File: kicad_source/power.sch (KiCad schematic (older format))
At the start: 19 parts, among them Q1 2N7002, Q2 2N7002, Q5 NTR4171P, SW3 SWITCH_INV, U1 TPS383X, U2 MCP73831, U3 TPS736XX

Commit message: updated power circuit
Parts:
- removed C1: 1u, capacitors:C_0603, symbol devices:C_0603
- removed D1: yellow, LEDs:LED_0603, symbol devices:Led_Small
- removed D5: MBR120, diodes:SOD-123, symbol devices:D_Schottky_Small
- removed F1: SF-1206S050, fuse_holders_and_fuses:Fuse_SMD1206_Reflow, symbol devices:F_Small
- removed Q1, Q2: 2N7002, SOT_TO:SOT-23, symbol devices:Q_NMOS_GSD
- removed Q5: NTR4171P, SOT_TO:SOT-23, symbol devices:Q_PMOS_GSD
- removed R1, R24: 4k7, resistors:R_0603, symbol devices:R_1206
- removed R5: 10k, resistors:R_0603, symbol devices:R_1206
- removed R7: 2k5, resistors:R_0603, symbol devices:R_1206
- removed U1: TPS383X, SOT_TO:SOT-23, symbol IC_voltage_supervisor:TPS383X
- removed U2: MCP73831, SOT_TO:SOT-23-5, symbol IC_batterycharger:MCP73831
- added BT?: Keystone 1043, MECH_battery_holder:KEYSTONE_1043, symbol devices:Battery
- added C? (x3): 1u, capacitors:C_0603, symbol devices:C_0603
- added C?: 100u/6.3V, capacitors:TantalC_SizeD_EIA-7343_Reflow, symbol devices:CP_Small
- added D? (x2): D_Small, symbol devices:D_Small
- added D?: D_Schottky_Small, symbol devices:D_Schottky_Small
- added R?: 150k, resistors:R_0603, symbol devices:R_0603
- added U?: TPS736XX, SOT_TO:SOT-23-5, symbol voltage-regulators:TPS736XX
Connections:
- net labels added: +1V8, 1V8_EN, VDD_CORE_EN
- net labels removed: +BATT, CHR_100MA, CHR_500MA, PROG
- wire segments 57 -> 46
- no-connect marks 2 -> 3
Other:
- note added: "use TPS73618DBVT\nfixed voltage 1.8 V"
- note added: "use TPS73633DBVT\nfixed voltage 3.3 V"
- note removed: "use MCP73832-2ACI/OT (4.2 V)"
- note removed: "use TPS3839G33DBZR\nthreshold voltage 3.08 V"
- note removed: "use TPS73630DBVT\nfixed voltage 3.0 V"
- moved on the sheet: BT1, C12, C2, C7, SW3, U3

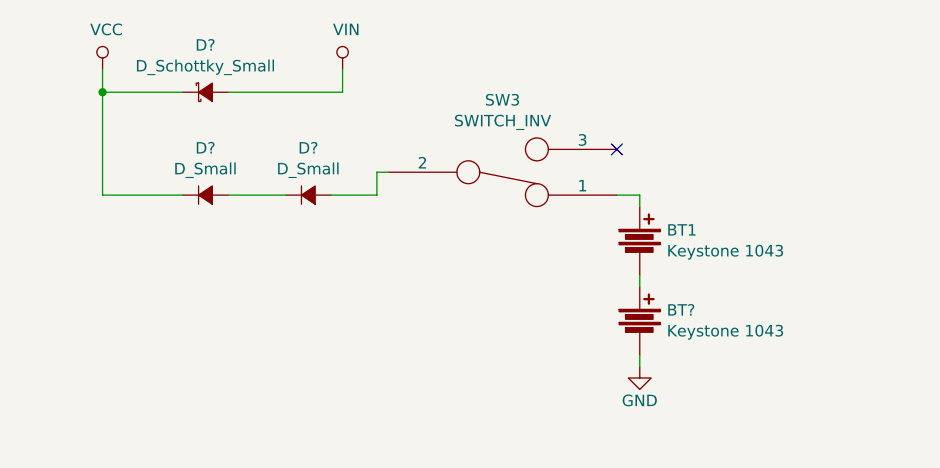
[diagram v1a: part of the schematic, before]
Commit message: added flash, JTAG connector and display to schematic
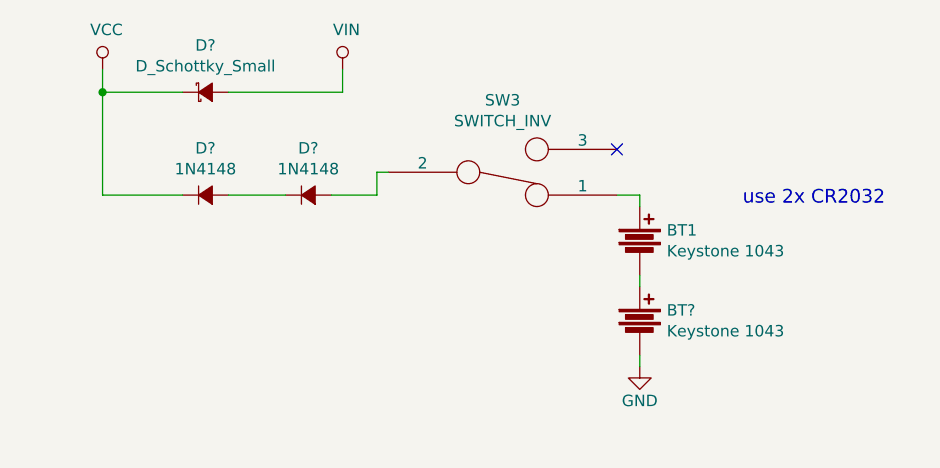
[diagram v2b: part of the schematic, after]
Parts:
- D? (x2): value D_Small -> 1N4148
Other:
- note added: "use 2x CR2032"
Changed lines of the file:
@@
 P 5500 1800
 F 0 "D?" H 5500 2005 50  0000 C CNN
-F 1 "D_Small" H 5500 1914 50  0000 C CNN
+F 1 "1N4148" H 5500 1914 50  0000 C CNN
 F 2 "" V 5500 1800 50  0000 C CNN
 F 3 "" V 5500 1800 50  0000 C CNN
@@
 P 5050 1800
 F 0 "D?" H 5050 2005 50  0000 C CNN
-F 1 "D_Small" H 5050 1914 50  0000 C CNN
+F 1 "1N4148" H 5050 1914 50  0000 C CNN
 F 2 "" V 5050 1800 50  0000 C CNN
 F 3 "" V 5050 1800 50  0000 C CNN
@@
 Wire Wire Line
 	6950 2500 6950 2550
+Text Notes 7400 1850 0    60   ~ 0
+use 2x CR2032
 $EndSCHEMATC

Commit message: added nfc part, generated schematic pdf
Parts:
- gave numbers to parts that had none: 10
- renumbered C2 to C32, C7 to C35, C12 to C37, SW3 to SW5, U3 to U5

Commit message: started placement
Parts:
- D7: value D_Schottky_Small -> MBR0530; footprint (none) -> diodes:SOD-123
- D8, D9: footprint (none) -> diodes:SOD-123
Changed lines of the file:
@@
 F 0 "D9" H 5500 2005 50  0000 C CNN
 F 1 "1N4148" H 5500 1914 50  0000 C CNN
-F 2 "" V 5500 1800 50  0000 C CNN
+F 2 "diodes:SOD-123" V 5500 1800 50  0001 C CNN
 F 3 "" V 5500 1800 50  0000 C CNN
 	1    5500 1800
@@
 F 0 "D8" H 5050 2005 50  0000 C CNN
 F 1 "1N4148" H 5050 1914 50  0000 C CNN
-F 2 "" V 5050 1800 50  0000 C CNN
+F 2 "diodes:SOD-123" V 5050 1800 50  0001 C CNN
 F 3 "" V 5050 1800 50  0000 C CNN
 	1    5050 1800
@@
 P 5050 1350
 F 0 "D7" H 5050 1555 50  0000 C CNN
-F 1 "D_Schottky_Small" H 5050 1464 50  0000 C CNN
-F 2 "" V 5050 1350 50  0000 C CNN
+F 1 "MBR0530" H 5050 1464 50  0000 C CNN
+F 2 "diodes:SOD-123" V 5050 1350 50  0001 C CNN
 F 3 "" V 5050 1350 50  0000 C CNN
 	1    5050 1350

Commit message: made first placement
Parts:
- BT1, BT2: value Keystone 1043 -> 79523141; footprint MECH_battery_holder:KEYSTONE_1043 -> MECH_battery_holder:Wuerth_WA-BCMC_79523141
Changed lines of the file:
@@
 AR Path="/5EB35F1D/5CB4F961" Ref="BT1"  Part="1"
 F 0 "BT1" H 7068 2046 50  0000 L CNN
-F 1 "Keystone 1043" H 7068 1955 50  0000 L CNN
-F 2 "MECH_battery_holder:KEYSTONE_1043" V 6950 2040 50  0001 C CNN
+F 1 "79523141" H 7068 1955 50  0000 L CNN
+F 2 "MECH_battery_holder:Wuerth_WA-BCMC_79523141" V 6950 2040 50  0001 C CNN
 F 3 "" V 6950 2040 50  0000 C CNN
 	1    6950 2000
@@
 AR Path="/5EB35F1D/5ECE9E11" Ref="BT2"  Part="1"
 F 0 "BT2" H 7068 2396 50  0000 L CNN
-F 1 "Keystone 1043" H 7068 2305 50  0000 L CNN
-F 2 "MECH_battery_holder:KEYSTONE_1043" V 6950 2390 50  0001 C CNN
+F 1 "79523141" H 7068 2305 50  0000 L CNN
+F 2 "MECH_battery_holder:Wuerth_WA-BCMC_79523141" V 6950 2390 50  0001 C CNN
 F 3 "" V 6950 2390 50  0000 C CNN
 	1    6950 2350

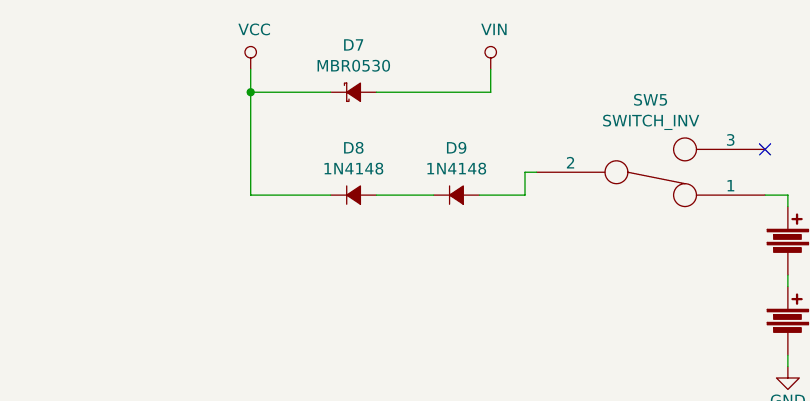
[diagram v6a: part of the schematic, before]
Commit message: changed diodes to smaller footprint, connected all lines in layout, updated images
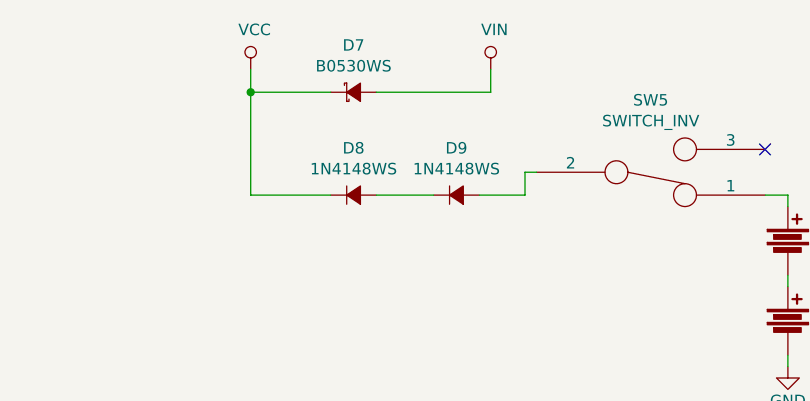
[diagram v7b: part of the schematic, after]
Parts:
- D7: value MBR0530 -> B0530WS; footprint diodes:SOD-123 -> diodes:SOD-323
- D8, D9: value 1N4148 -> 1N4148WS; footprint diodes:SOD-123 -> diodes:SOD-323
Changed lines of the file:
@@
 P 5500 1800
 F 0 "D9" H 5500 2005 50  0000 C CNN
-F 1 "1N4148" H 5500 1914 50  0000 C CNN
-F 2 "diodes:SOD-123" V 5500 1800 50  0001 C CNN
+F 1 "1N4148WS" H 5500 1914 50  0000 C CNN
+F 2 "diodes:SOD-323" V 5500 1800 50  0001 C CNN
 F 3 "" V 5500 1800 50  0000 C CNN
 	1    5500 1800
@@
 P 5050 1800
 F 0 "D8" H 5050 2005 50  0000 C CNN
-F 1 "1N4148" H 5050 1914 50  0000 C CNN
-F 2 "diodes:SOD-123" V 5050 1800 50  0001 C CNN
+F 1 "1N4148WS" H 5050 1914 50  0000 C CNN
+F 2 "diodes:SOD-323" V 5050 1800 50  0001 C CNN
 F 3 "" V 5050 1800 50  0000 C CNN
 	1    5050 1800
@@
 P 5050 1350
 F 0 "D7" H 5050 1555 50  0000 C CNN
-F 1 "MBR0530" H 5050 1464 50  0000 C CNN
-F 2 "diodes:SOD-123" V 5050 1350 50  0001 C CNN
+F 1 "B0530WS" H 5050 1464 50  0000 C CNN
+F 2 "diodes:SOD-323" V 5050 1350 50  0001 C CNN
 F 3 "" V 5050 1350 50  0000 C CNN
 	1    5050 1350

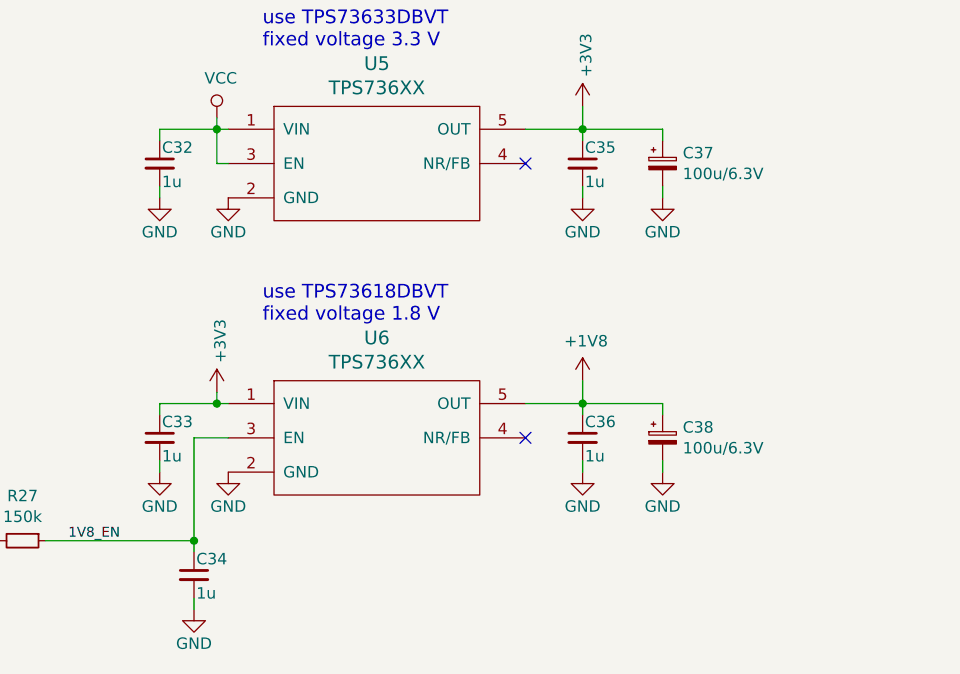
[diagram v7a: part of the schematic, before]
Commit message: corrected some part numbers
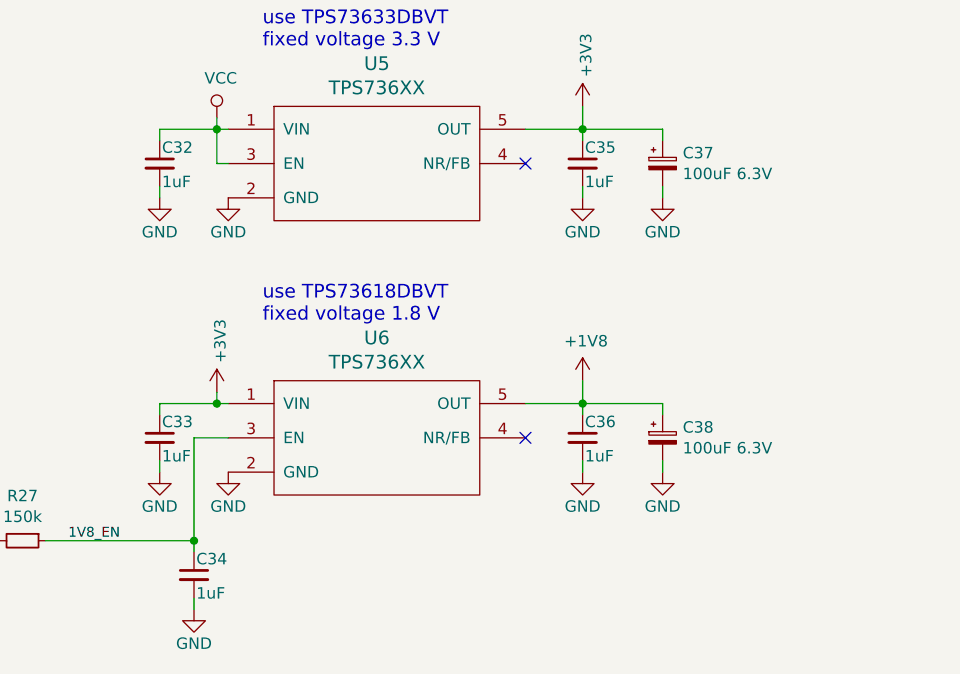
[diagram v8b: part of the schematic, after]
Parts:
- C32, C33, C34, C35, C36: value 1u -> 1uF
- C37, C38: value 100u/6.3V -> 100uF 6.3V
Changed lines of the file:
@@
 AR Path="/5EB35F1D/5CB4F8A0" Ref="C32"  Part="1"
 F 0 "C32" H 3360 4170 50  0000 L CNN
-F 1 "1u" H 3360 4020 50  0000 L CNN
+F 1 "1uF" H 3360 4020 50  0000 L CNN
 F 2 "capacitors:C_0603" H 3350 3950 50  0001 C CNN
 F 3 "" H 3350 4100 50  0000 C CNN
@@
 AR Path="/5EB35F1D/5CB4F8A7" Ref="C35"  Part="1"
 F 0 "C35" H 5210 4170 50  0000 L CNN
-F 1 "1u" H 5210 4020 50  0000 L CNN
+F 1 "1uF" H 5210 4020 50  0000 L CNN
 F 2 "capacitors:C_0603" H 5200 3950 50  0001 C CNN
 F 3 "" H 5200 4100 50  0000 C CNN
@@
 P 5550 4100
 F 0 "C37" H 5638 4146 50  0000 L CNN
-F 1 "100u/6.3V" H 5638 4055 50  0000 L CNN
+F 1 "100uF 6.3V" H 5638 4055 50  0000 L CNN
 F 2 "capacitors:TantalC_SizeD_EIA-7343_Reflow" H 5550 4100 50  0001 C CNN
 F 3 "" H 5550 4100 50  0000 C CNN
@@
 AR Path="/5EB35F1D/5EB83C46" Ref="C33"  Part="1"
 F 0 "C33" H 3360 5370 50  0000 L CNN
-F 1 "1u" H 3360 5220 50  0000 L CNN
+F 1 "1uF" H 3360 5220 50  0000 L CNN
 F 2 "capacitors:C_0603" H 3350 5150 50  0001 C CNN
 F 3 "" H 3350 5300 50  0000 C CNN
@@
 AR Path="/5EB35F1D/5EB83C50" Ref="C36"  Part="1"
 F 0 "C36" H 5210 5370 50  0000 L CNN
-F 1 "1u" H 5210 5220 50  0000 L CNN
+F 1 "1uF" H 5210 5220 50  0000 L CNN
 F 2 "capacitors:C_0603" H 5200 5150 50  0001 C CNN
 F 3 "" H 5200 5300 50  0000 C CNN
@@
 P 5550 5300
 F 0 "C38" H 5638 5346 50  0000 L CNN
-F 1 "100u/6.3V" H 5638 5255 50  0000 L CNN
+F 1 "100uF 6.3V" H 5638 5255 50  0000 L CNN
 F 2 "capacitors:TantalC_SizeD_EIA-7343_Reflow" H 5550 5300 50  0001 C CNN
 F 3 "" H 5550 5300 50  0000 C CNN
@@
 AR Path="/5EB35F1D/5EC53831" Ref="C34"  Part="1"
 F 0 "C34" H 3510 5970 50  0000 L CNN
-F 1 "1u" H 3510 5820 50  0000 L CNN
+F 1 "1uF" H 3510 5820 50  0000 L CNN
 F 2 "capacitors:C_0603" H 3500 5750 50  0001 C CNN
 F 3 "" H 3500 5900 50  0000 C CNN
